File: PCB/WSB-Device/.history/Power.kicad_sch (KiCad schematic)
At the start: 34 parts, among them P2 USB_C_Plug_USB2.0, SW1 SW_SPST_4_PIN, U1 ESP32-C6-MINI-1, U2 74LV1T34, U3 NCP187, U4 TPD2E2U06DRL

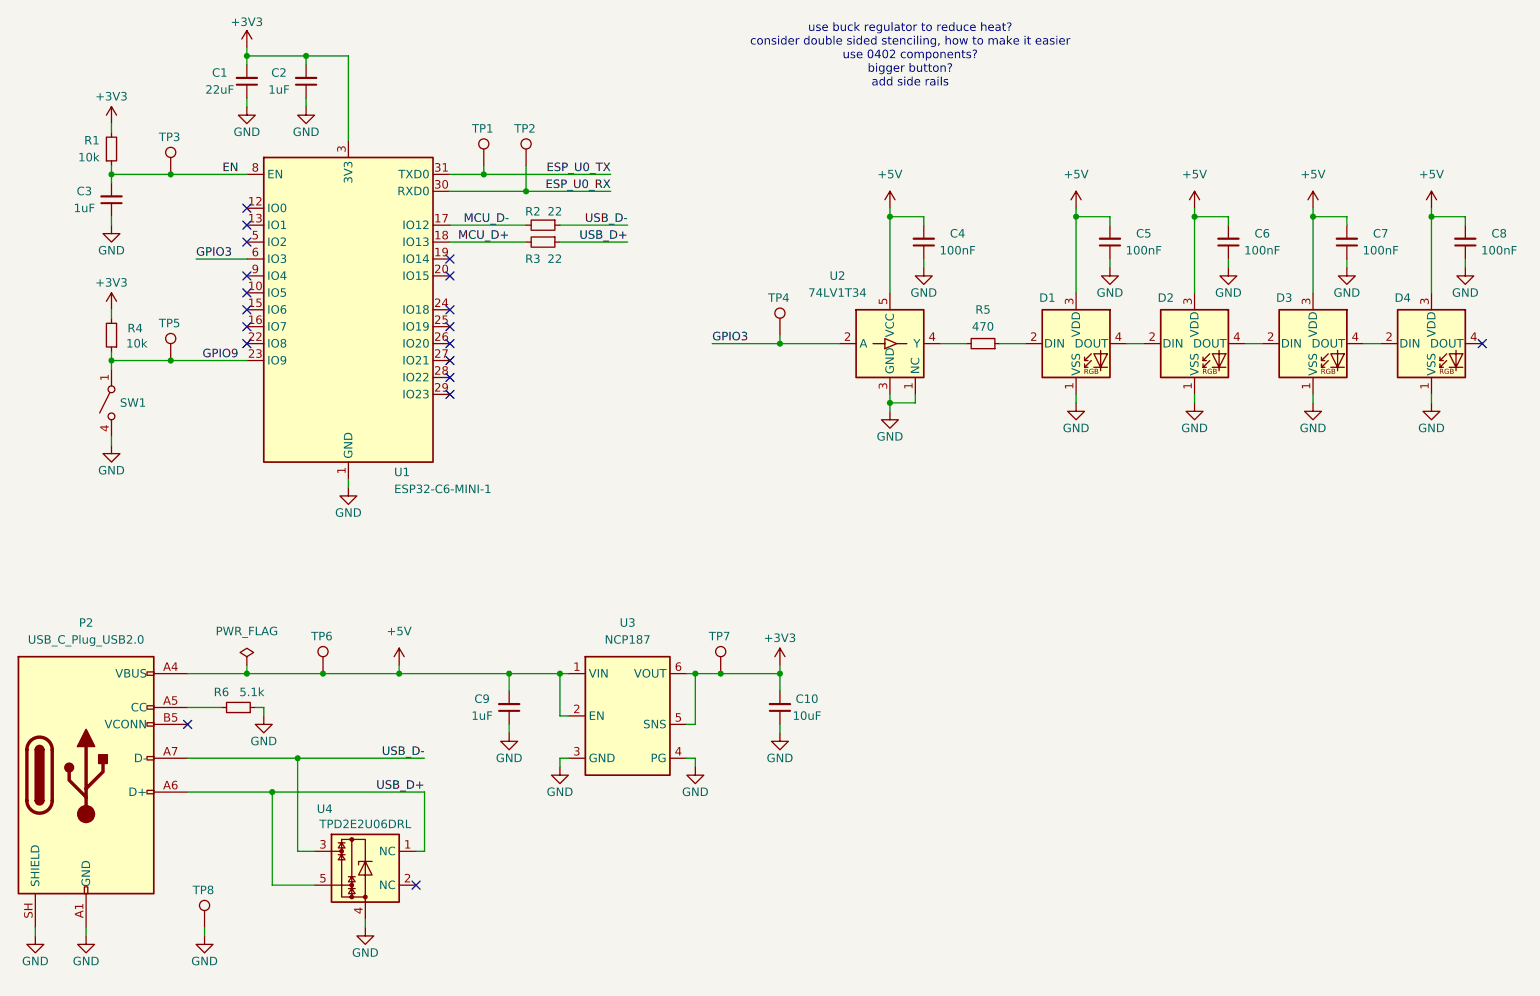
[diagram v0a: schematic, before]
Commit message: -Changed USB connector -Moved LEDs in behind board edge -Changed to smaller test points
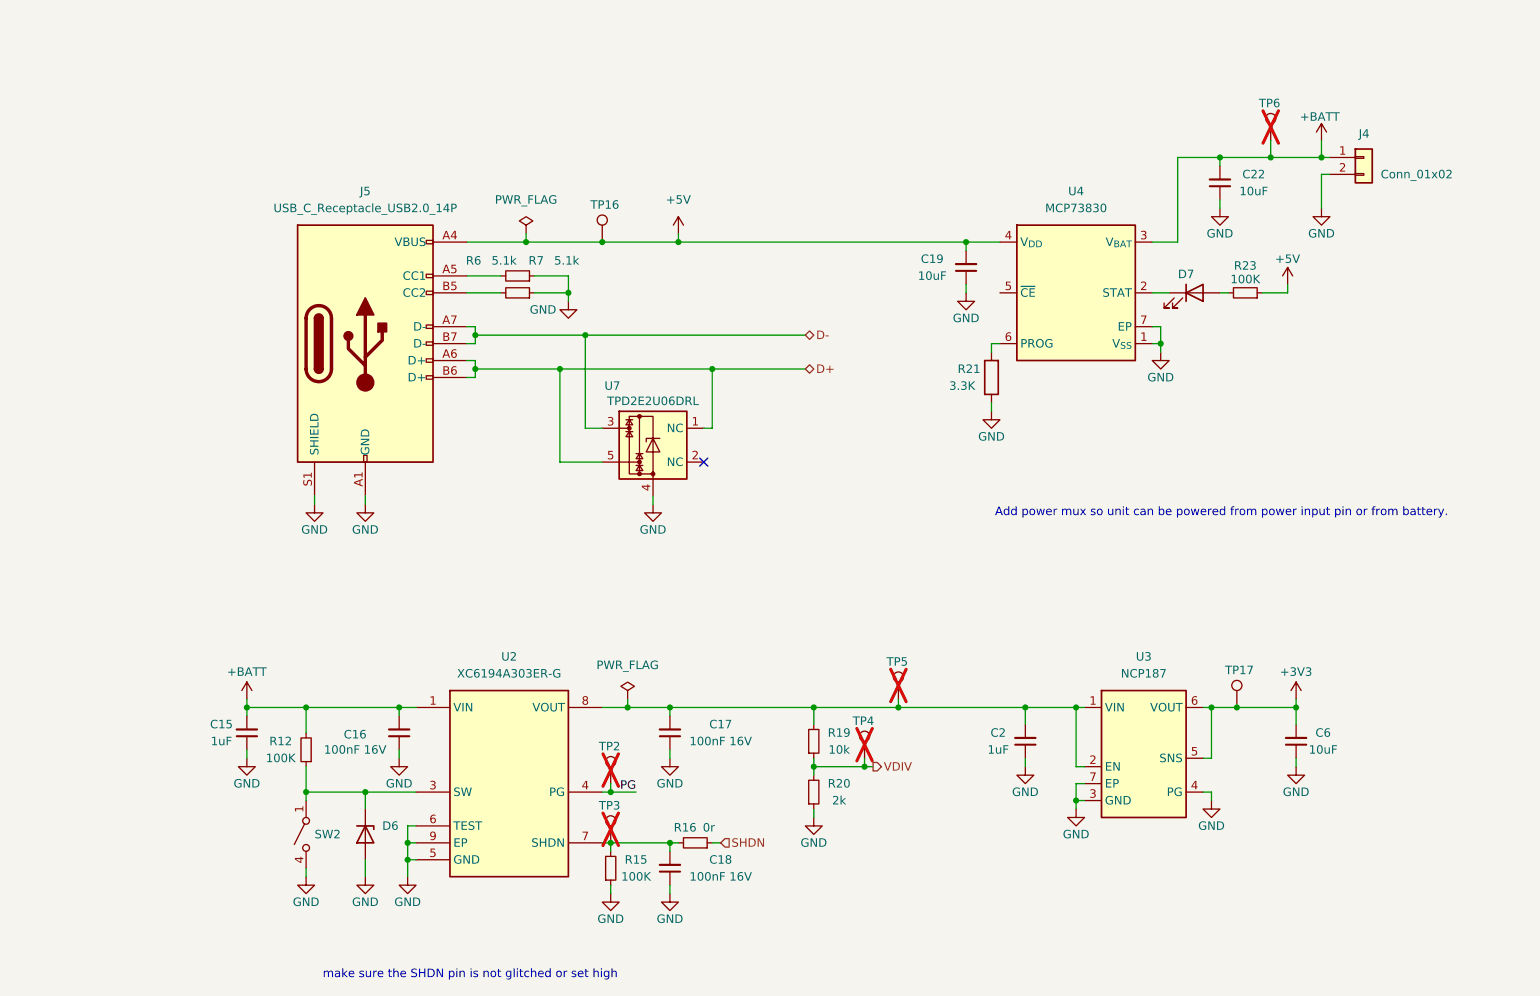
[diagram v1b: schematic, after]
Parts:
- removed C1: 22uF, Capacitor_SMD:C_0603_1608Metric, symbol Device:C_Small
- removed C10: 10uF, Capacitor_SMD:C_0603_1608Metric, symbol Device:C_Small
- removed C3, C9: 1uF, Capacitor_SMD:C_0402_1005Metric, symbol Device:C_Small
- removed C4, C5, C7, C8: 100nF, Capacitor_SMD:C_0201_0603Metric, symbol Device:C_Small
- removed D1, D2, D3, D4: (no value), EN_Designs-Footprints:XL-3210RGBC-2812B, symbol LED:SK6812
- removed P2: USB_C_Plug_USB2.0, EN_Designs-Footprints:GT-USB-8016A, symbol Connector:USB_C_Plug_USB2.0
- removed R1, R4: 10k, Resistor_SMD:R_0201_0603Metric, symbol Device:R_Small
- removed R2, R3: 22, Resistor_SMD:R_0201_0603Metric, symbol Device:R_Small
- removed R5: 470, Resistor_SMD:R_0201_0603Metric, symbol Device:R_Small
- removed SW1: SW_SPST_4_PIN, EN_Designs-Footprints:1TS026A-2300-0553-CT, symbol EN_Designs-Symbols:SW_SPST_4_PIN
- removed TP1, TP7, TP8: TestPoint, EN_Designs-Footprints:TestPoint_Pad_D0.5mm, symbol Connector:TestPoint
- removed U1: ESP32-C6-MINI-1, RF_Module:ESP32-C6-MINI-1, symbol RF_Module:ESP32-C6-MINI-1
- removed U2: 74LV1T34, EN_Designs-Footprints:X2SON5_0.8x0.8mm_SOT1226, symbol EN_Designs-Symbols:74LV1T34
- removed U4: TPD2E2U06DRL, Package_TO_SOT_SMD:SOT-553, symbol Power_Protection:TPD2E2U06DRL
- added C15: 1uF, Capacitor_SMD:C_0603_1608Metric, symbol Device:C_Small
- added C16, C17, C18: 100nF 16V, Capacitor_SMD:C_0402_1005Metric, symbol Device:C_Small
- added C19, C22: 10uF, Capacitor_SMD:C_0603_1608Metric, symbol Device:C_Small
- added D6: D_Zener, Diode_SMD:D_SOD-323, symbol Device:D_Zener
- added D7: LED, LED_SMD:LED_0603_1608Metric, symbol Device:LED
- added J4: Conn_01x02, Connector_JST:JST_PH_S2B-PH-SM4-TB_1x02-1MP_P2.00mm_Horizontal, symbol Connector_Generic:Conn_01x02
- added J5: USB_C_Receptacle_USB2.0_14P, Connector_USB:USB_C_Receptacle_G-Switch_GT-USB-7010ASV, symbol Connector:USB_C_Receptacle_USB2.0_14P
- added R12, R15, R23: 100K, Resistor_SMD:R_0402_1005Metric, symbol Device:R_Small
- added R16: 0r, Resistor_SMD:R_0402_1005Metric, symbol Device:R_Small
- added R19: 10k, Resistor_SMD:R_0402_1005Metric, symbol Device:R_Small
- added R20: 2k, Resistor_SMD:R_0402_1005Metric, symbol Device:R_Small
- added R21: 3.3K, Resistor_SMD:R_0402_1005Metric, symbol Device:R
- added R7: 5.1k, Resistor_SMD:R_0201_0603Metric, symbol Device:R_Small
- added SW2: SW_SPST_4_PIN, EN_Designs-Footprints:1TS026A-2300-0553-CT, symbol EN_Designs-Symbols:SW_SPST_4_PIN
- added TP16, TP17: TestPoint, EN_Designs-Footprints:TestPoint_Pad_D1.0mm, symbol Connector:TestPoint
- added U2: XC6194A303ER-G, EN_Designs-Footprints:XC6194_USP-8B06, symbol EN_Designs-Symbols:XC6194A303ER-G
- added U4: MCP73830, EN_Designs-Footprints:TDFN-6-1EP_2x2mm_P0.5mm_EP1.6x0.6mm_ThermalVias, symbol EN_Designs-Symbols:MCP73830/L
- added U7: TPD2E2U06DRL, Package_TO_SOT_SMD:SOT-553, symbol Power_Protection:TPD2E2U06DRL
- C6: value 100nF -> 10uF; footprint Capacitor_SMD:C_0201_0603Metric -> Capacitor_SMD:C_0603_1608Metric
- TP2, TP3, TP4, TP5, TP6: footprint EN_Designs-Footprints:TestPoint_Pad_D0.5mm -> TestPoint:TestPoint_Pad_D1.0mm; now not fitted
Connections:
- net +3V3: now also C6.2, TP17.1; no longer C2.2
- net +5V: now also C19.2, J5.A4 (VBUS), J5.A9 (VBUS), J5.B4 (VBUS), J5.B9 (VBUS), R23.1, TP16.1, U4.4 (V_{DD}); no longer C6.2, TP6.1, U3.1 (VIN), U3.2 (EN)
- net at R6.2: now also J5.A5 (CC1)
- net EN: no longer names the net of TP3.1
- net EN: now also C18.2, R15.2, R16.2, U2.7 (SHDN)
- net EP renamed GND
- net GND: now also C15.1, C16.1, C17.1, C18.1, C19.1, C22.1, D6.2 (A), J4.2 (Pin_2), J5.A1 (GND), J5.A12 (GND), J5.B1 (GND), J5.B12 (GND), J5.S1 (SHIELD), R15.1, R20.1, R21.1, R7.1, SW2.3 (B), SW2.4 (B), U2.5 (GND), U2.6 (TEST), U2.9 (EP), U4.1 (V_{SS}), U4.7 (EP), U7.4
- net ESP_U0_RX renamed PG
- net PG: now also U2.4 (PG)
- net GPIO3 renamed VDIV
- net VDIV: now also R19.1, R20.2
- net GPIO9: no longer names the net of TP5.1
- net GPIO9: now also C2.2, U3.1 (VIN), U3.2 (EN), C17.2, R19.2, U2.8 (VOUT)
- new net: D7.2 (A), R23.2
- new net: D6.1 (K), R12.1, SW2.1 (A), SW2.2 (A), U2.3 (SW)
- new net: J5.B5 (CC2), R7.2
- new net: R21.2, U4.6 (PROG)
- new net: D7.1 (K), U4.2 (STAT)
- new net +BATT: C15.2, C16.2, C22.2, J4.1 (Pin_1), R12.2, TP6.1, U2.1 (VIN), U4.3 (V_{BAT})
- new net D+: J5.A6 (D+), J5.B6 (D+), U7.1 (NC), U7.5
- new net D-: J5.A7 (D-), J5.B7 (D-), U7.3
- new net SHDN: R16.1
- no-connect marks 19 -> 1
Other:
- note added: "Add power mux so unit can be powered from power input pin or from battery."
- note added: "make sure the SHDN pin is not glitched or set high"
- note removed: "use buck regulator to reduce heat? consider double sided stenciling, how to make it easier use 0402 components? bigger button? add side rails"
